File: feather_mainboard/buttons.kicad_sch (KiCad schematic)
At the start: 4 parts

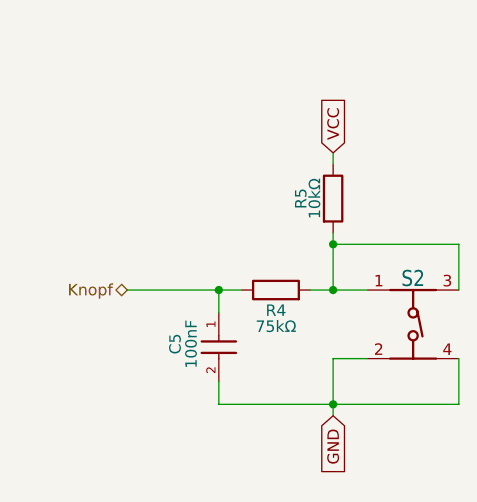
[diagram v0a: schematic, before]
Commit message: finished microcontroller and microsd card subsheets. TODO: button subsheets and internal connections
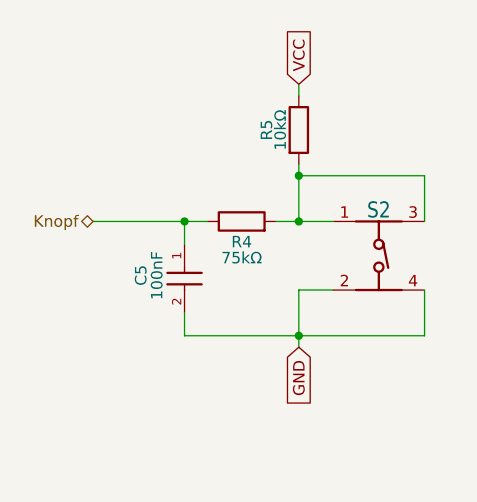
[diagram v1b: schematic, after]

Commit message: schematic is almost done (check TODOs in schematic file)
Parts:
- added C7, C9: 100nF, footprints:WCAP-CSGP_1210_H2.0, symbol WCAP-CSGP_1210_H2.0:WCAP-CSGP_1210_H2.0
- added R4, R8: 75kΩ, Resistor_SMD:R_0805_2012Metric_Pad1.20x1.40mm_HandSolder, symbol Device:R
- added R5, R9: 10kΩ, Resistor_SMD:R_0805_2012Metric_Pad1.20x1.40mm_HandSolder, symbol Device:R
- added S2, S4: 430182050816, footprints:430182050816, symbol Projektarbeit_button:430182050816
- renumbered C5 to C8, R4 to R6, R5 to R7, S2 to S3
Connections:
- net GND: now also C7.2, C9.2, S2.2, S2.4, S4.2, S4.4
- net VCC: now also R5.1, R9.1
- net Knopf renamed Button_2
- new net: R4.2, R5.2, S2.1, S2.3
- new net: R8.2, R9.2, S4.1, S4.3
- new net Button_1: C7.1, R4.1
- new net Button_3: C9.1, R8.1
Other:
- moved on the sheet: C8, R6, R7, S3

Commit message: changed footprints location to match the new folder. TODO: check if the path is working on another computer
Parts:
- C7, C8, C9: footprint footprints:WCAP-CSGP_1210_H2.0 -> Custom footprints:WCAP-CSGP_1210_H2.0
- S2, S3, S4: footprint footprints:430182050816 -> Custom footprints:430182050816
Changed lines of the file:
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@@
 	)
 	(symbol
+		(lib_name "430182050816_1")
 		(lib_id "Projektarbeit_button:430182050816")
 		(at 198.12 101.6 0)
@@
 			)
 		)
-		(property "Footprint" "footprints:430182050816"
+		(property "Footprint" "Custom footprints:430182050816"
 			(at 198.12 101.6 0)
 			(effects
@@
 			)
 		)
-		(property "Footprint" "footprints:430182050816"
+		(property "Footprint" "Custom footprints:430182050816"
 			(at 124.46 101.6 0)
 			(effects
@@
 			)
 		)
-		(property "Footprint" "footprints:WCAP-CSGP_1210_H2.0"
+		(property "Footprint" "Custom footprints:WCAP-CSGP_1210_H2.0"
 			(at 102.87 101.6 0)
 			(effects
@@
 	)
 	(symbol
+		(lib_name "WCAP-CSGP_1210_H2.0_1")
 		(lib_id "WCAP-CSGP_1210_H2.0:WCAP-CSGP_1210_H2.0")
 		(at 176.53 101.6 270)
@@
 			)
 		)
-		(property "Footprint" "footprints:WCAP-CSGP_1210_H2.0"
+		(property "Footprint" "Custom footprints:WCAP-CSGP_1210_H2.0"
 			(at 176.53 101.6 0)
 			(effects
@@
 	)
 	(symbol
+		(lib_name "430182050816_2")
 		(lib_id "Projektarbeit_button:430182050816")
 		(at 161.29 101.6 0)
@@
 			)
 		)
-		(property "Footprint" "footprints:430182050816"
+		(property "Footprint" "Custom footprints:430182050816"
 			(at 161.29 101.6 0)
 			(effects
@@
 	)
 	(symbol
+		(lib_name "WCAP-CSGP_1210_H2.0_2")
 		(lib_id "WCAP-CSGP_1210_H2.0:WCAP-CSGP_1210_H2.0")
 		(at 139.7 101.6 270)
@@
 			)
 		)
-		(property "Footprint" "footprints:WCAP-CSGP_1210_H2.0"
+		(property "Footprint" "Custom footprints:WCAP-CSGP_1210_H2.0"
 			(at 139.7 101.6 0)
 			(effects

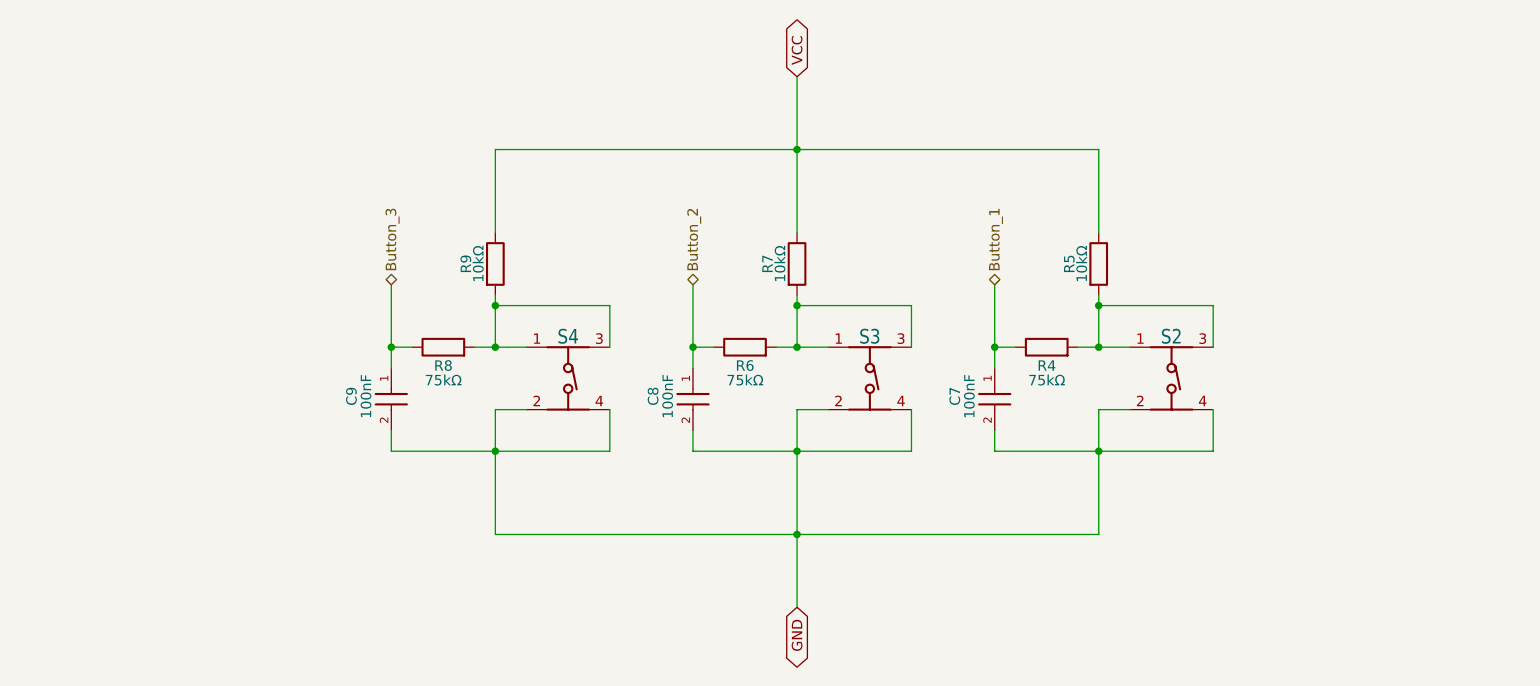
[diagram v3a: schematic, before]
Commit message: added daughter board
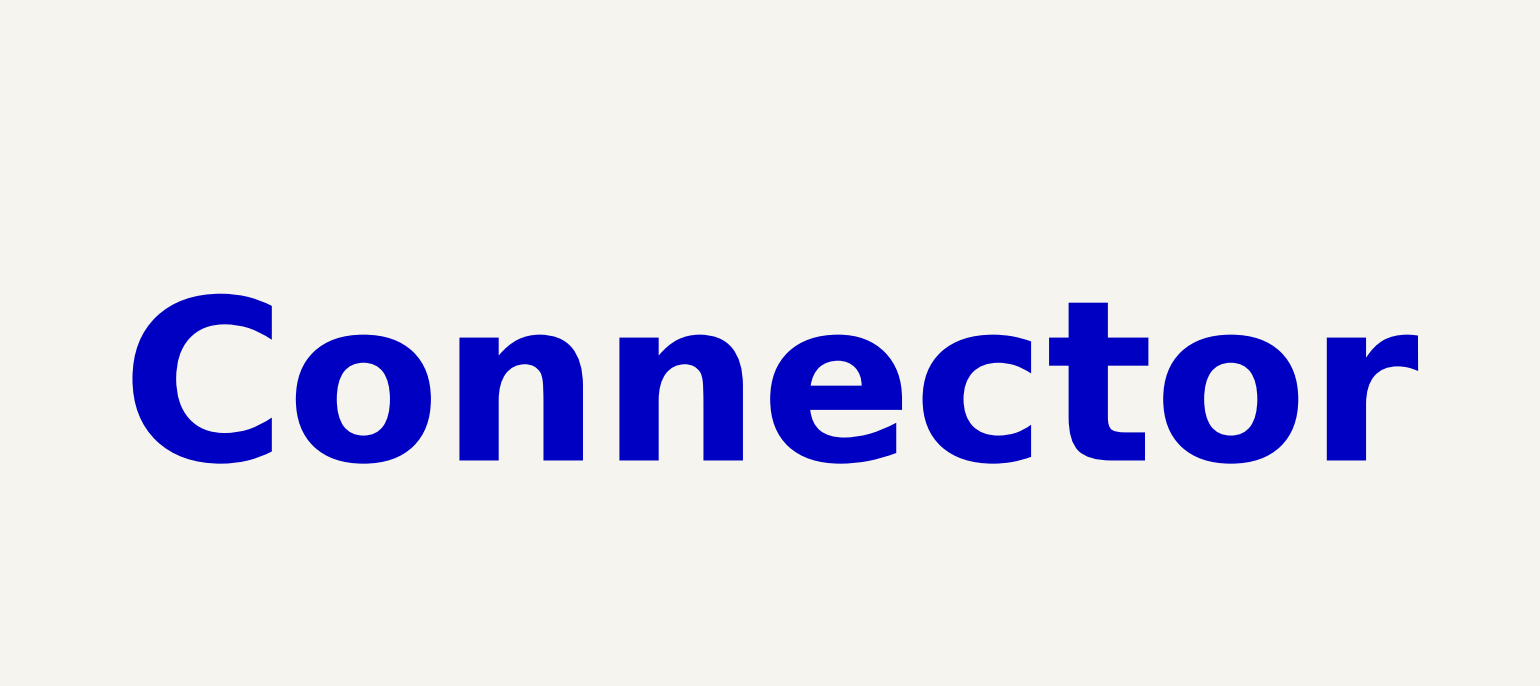
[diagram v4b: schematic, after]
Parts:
- removed C7, C8, C9: 100nF, Custom footprints:WCAP-CSGP_1210_H2.0, symbol WCAP-CSGP_1210_H2.0:WCAP-CSGP_1210_H2.0
- removed R4, R6, R8: 75kΩ, Resistor_SMD:R_0805_2012Metric_Pad1.20x1.40mm_HandSolder, symbol Device:R
- removed R5, R7, R9: 10kΩ, Resistor_SMD:R_0805_2012Metric_Pad1.20x1.40mm_HandSolder, symbol Device:R
- removed S2, S3, S4: 430182050816, Custom footprints:430182050816, symbol Projektarbeit_button:430182050816
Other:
- note added: "Connector"
